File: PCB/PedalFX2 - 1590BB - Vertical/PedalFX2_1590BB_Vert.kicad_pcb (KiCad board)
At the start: 2 copper layers, 109.5 x 40.1 mm, 12 parts, among them J1 Conn_01x04_Female, T1 ACJS-MHDR, T2 ACJS-MHDR, T3 54-00129

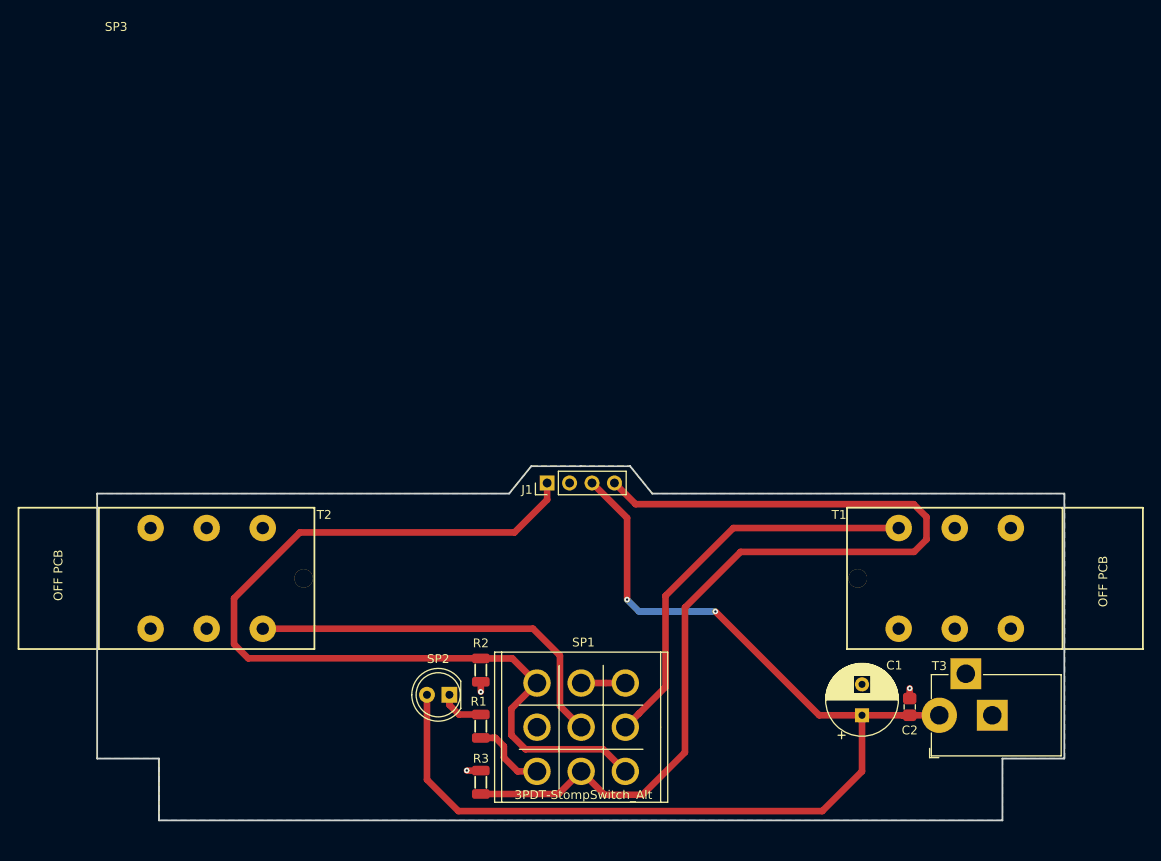
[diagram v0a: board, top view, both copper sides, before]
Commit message: 1590BB
1590BB variants in progress. Horizontal one finished, working on vertical. TRS jack footprint needs adjustment.
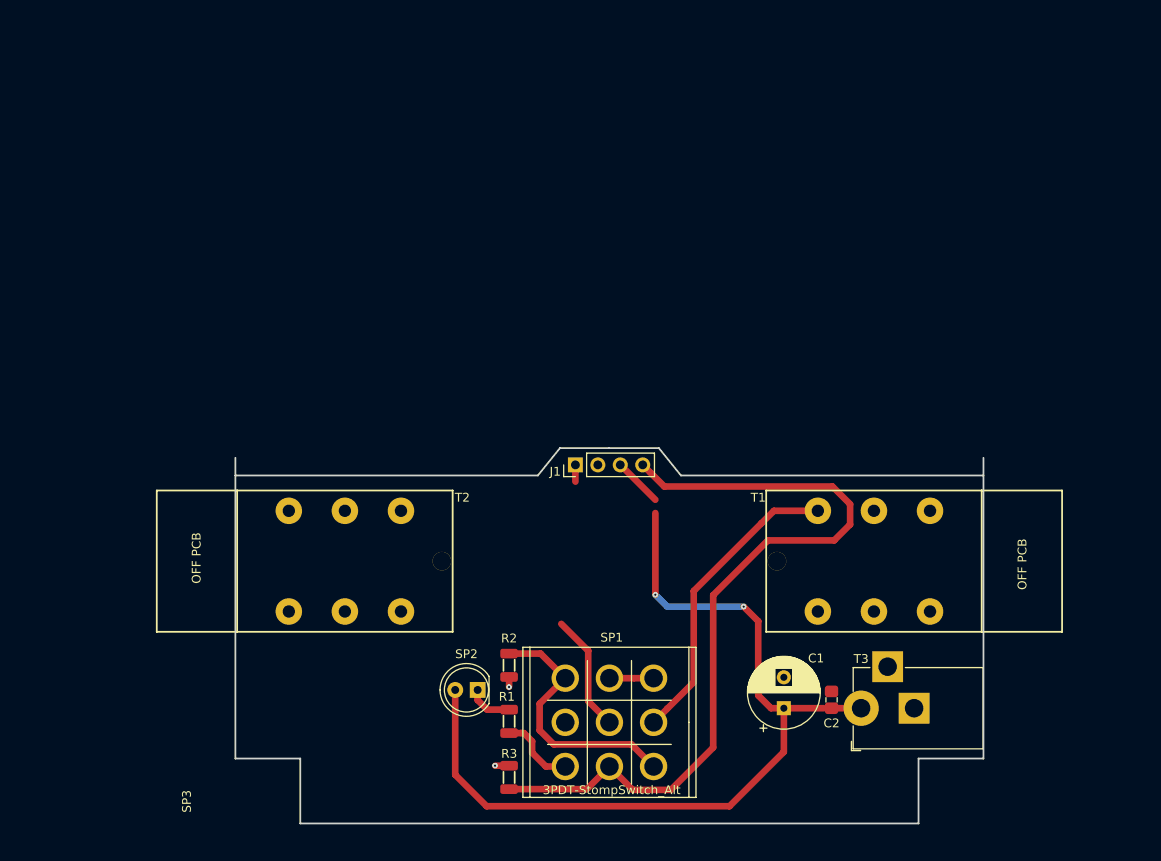
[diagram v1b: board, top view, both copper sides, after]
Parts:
- moved SP3 100.0 mm to (200.0, 150.0), turned to 90 degrees
- moved T2 15.8 mm to (128.1, 120.7)
- moved T1 9.36 mm to (187.9, 120.7)
- moved C2 8.89 mm to (183.2, 136.3)
- moved C1 8.89 mm to (177.8, 137.3)
- moved T3 8.89 mm to (186.5, 137.3)
- moved J1 3.80 mm to (154.2, 109.8)
- moved R2 3.25 mm to (146.6, 132.4)
- moved R1 3.25 mm to (146.6, 138.8)
- moved R3 3.25 mm to (146.6, 145.1)
- moved SP2 3.25 mm to (143.1, 135.2)
- moved SP1 3.25 mm to (158.0, 138.9)
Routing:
- net Net-(J1-Pad1): track 105.0 -> 31.1 mm
- net Net-(SP1-Pad5): track 44.0 -> 13.4 mm
- net Net-(J1-Pad4): track 113.7 -> 90.9 mm
- net +9V: track 124.2 -> 103.3 mm
- net Net-(SP1-Pad4): track 46.3 -> 34.6 mm
- net GND: track 3.88 -> 2.73 mm, vias 3 -> 2
- removed copper zone on B.Cu, net GND
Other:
- board size 109.5 x 40.1 mm -> 84.7 x 42.5 mm

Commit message: 1590BB Verticalk
Vertical variant completed, incorporated adjuistments to TRS footprint, others will be updated to follow.
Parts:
- moved T1 1.90 mm to (189.8, 120.7)
- moved T2 1.90 mm to (126.2, 120.7)
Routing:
- net Net-(J1-Pad1): track 31.1 -> 87.3 mm
- net Net-(SP1-Pad5): track 13.4 -> 34.0 mm
- net Net-(J1-Pad4): track 90.9 -> 94.3 mm
- net Net-(SP1-Pad4): track 34.6 -> 36.5 mm
- net +9V: track 103.3 -> 104.8 mm
- added copper zone on B.Cu, net GND
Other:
- outline, holes or cut-outs redrawn

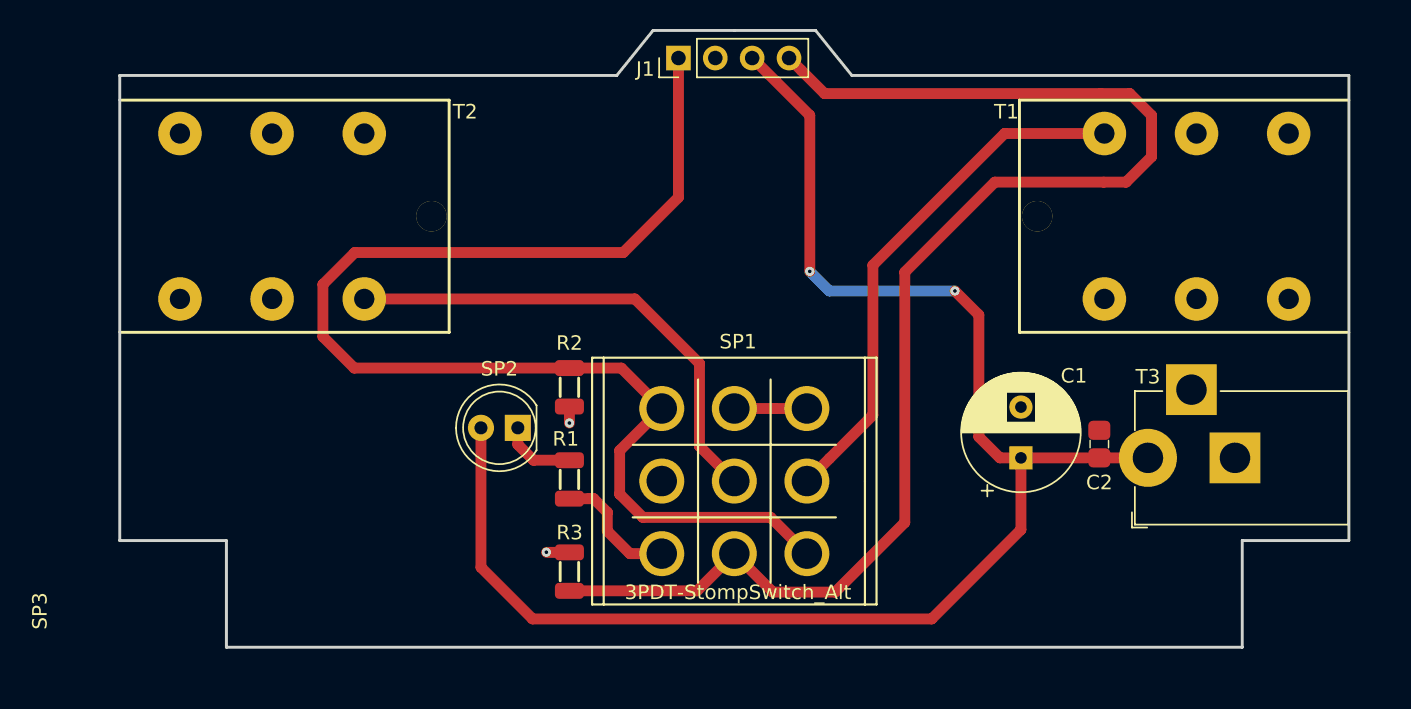
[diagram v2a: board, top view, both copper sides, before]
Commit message: Goofed
Goofed internal connector flipped and jacks not flush with housing. All fixed now, all boards redone.
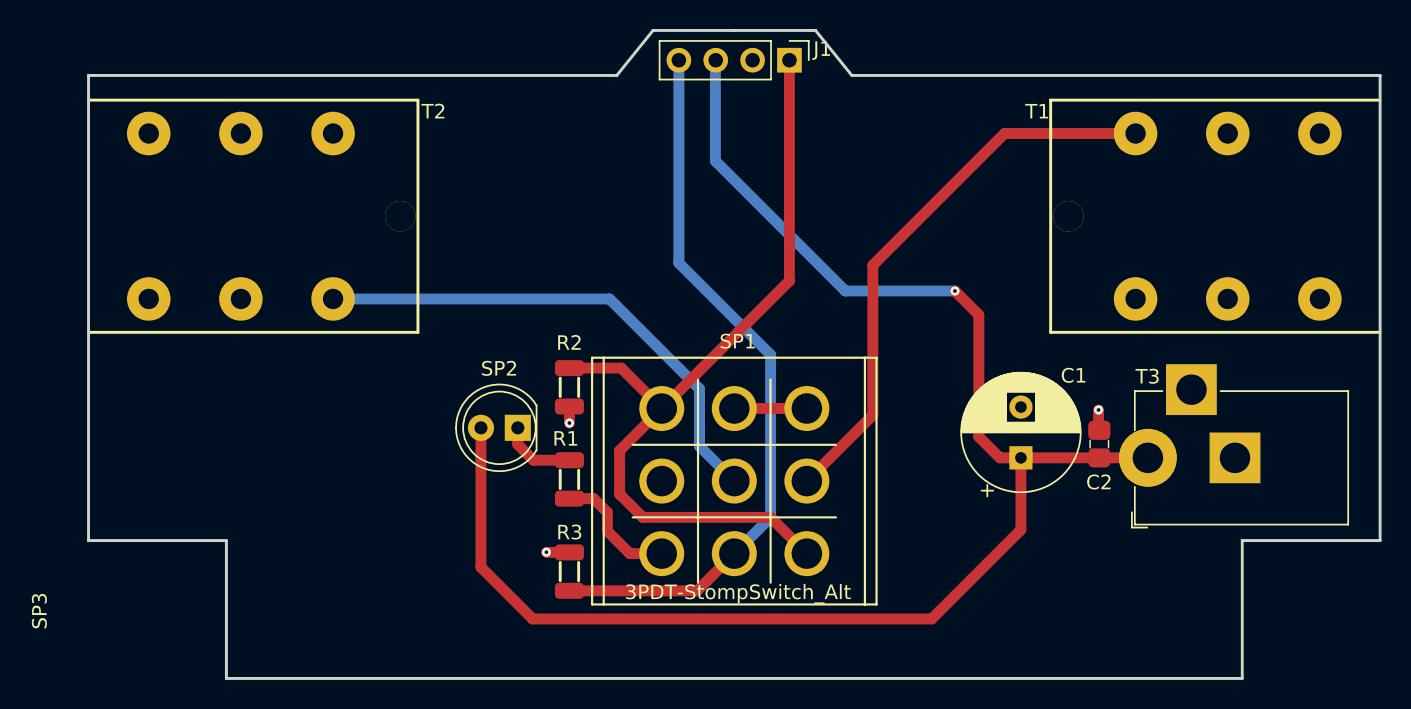
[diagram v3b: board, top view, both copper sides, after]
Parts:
- moved J1 7.65 mm to (161.8, 109.9), turned to 270 degrees
- moved T1 2.15 mm to (192.0, 120.7)
- moved T2 2.15 mm to (124.0, 120.7)
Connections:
- net Net-(J1-Pad1) renamed /IN
- net Net-(J1-Pad4) renamed /OUT
- net Net-(SP1-Pad1) renamed /BYPASS
- net Net-(SP1-Pad4) renamed /Pedal_IN
- net Net-(SP1-Pad5) renamed /Pedal_OUT
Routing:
- net /OUT: track 94.3 -> 50.1 mm
- net /IN: track 87.3 -> 56.9 mm
- net /Pedal_IN: track 36.5 -> 38.6 mm
- net GND: track 2.73 -> 4.15 mm, vias 2 -> 3
- net /Pedal_OUT: track 34.0 -> 35.2 mm
- net +9V: track 104.8 -> 105.1 mm, vias 2 -> 1
- added copper zone on F.Cu, net GND
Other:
- board size 84.7 x 42.5 mm -> 89 x 44.7 mm
